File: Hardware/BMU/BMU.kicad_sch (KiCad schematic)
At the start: 5 parts, among them J1 Conn_01x02, J2 Conn_01x04, J3 Conn_01x02, J4 Conn_01x03, J5 Conn_01x03

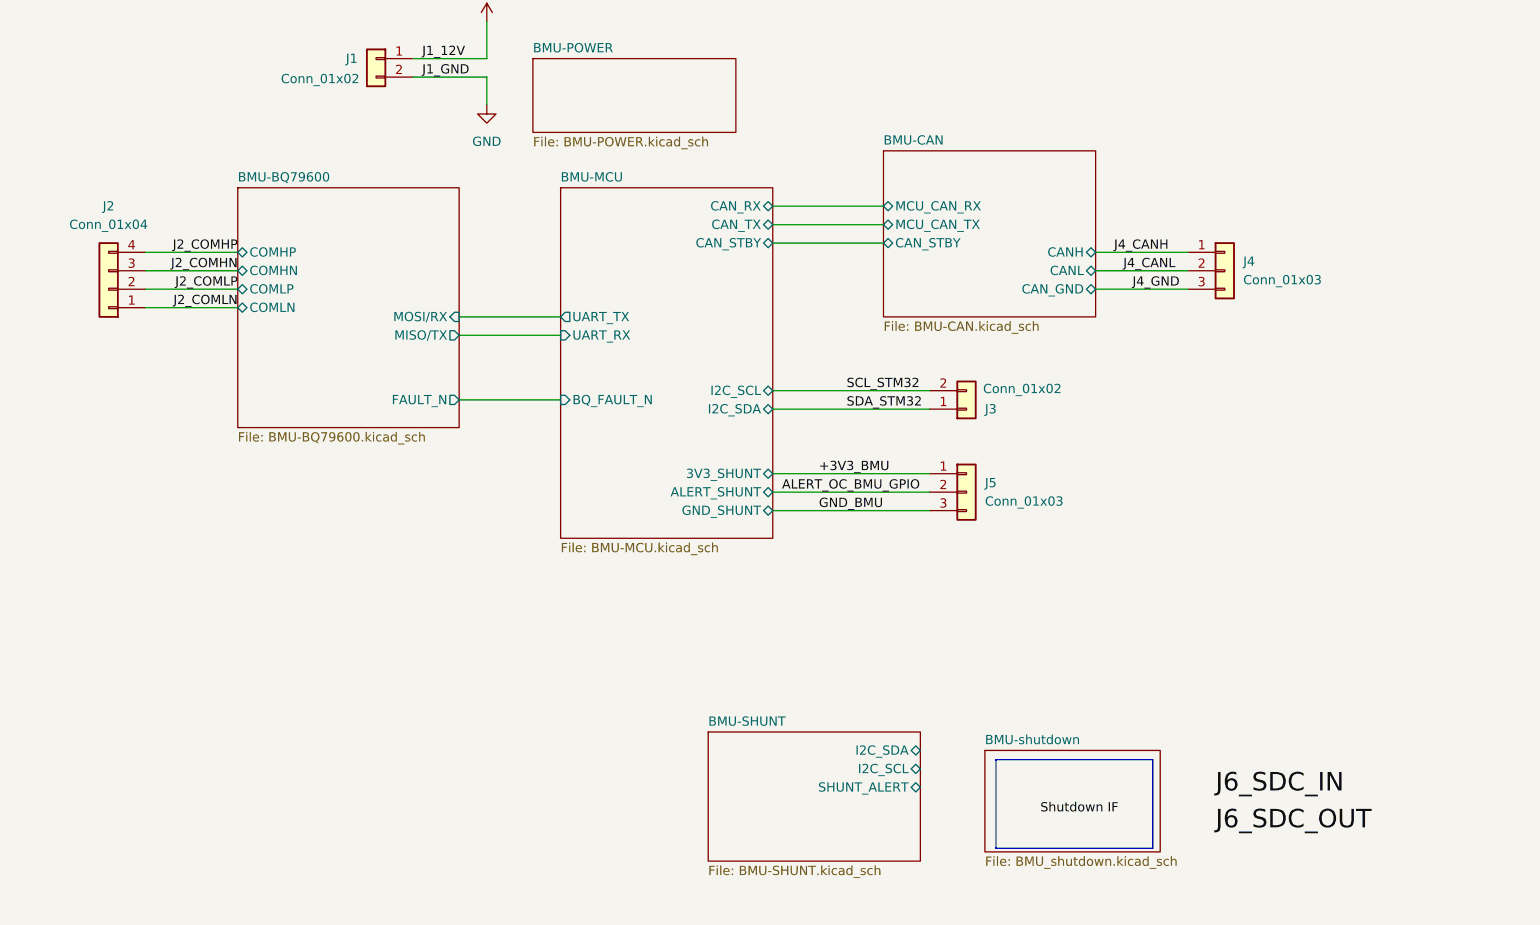
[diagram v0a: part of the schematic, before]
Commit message: change CAN
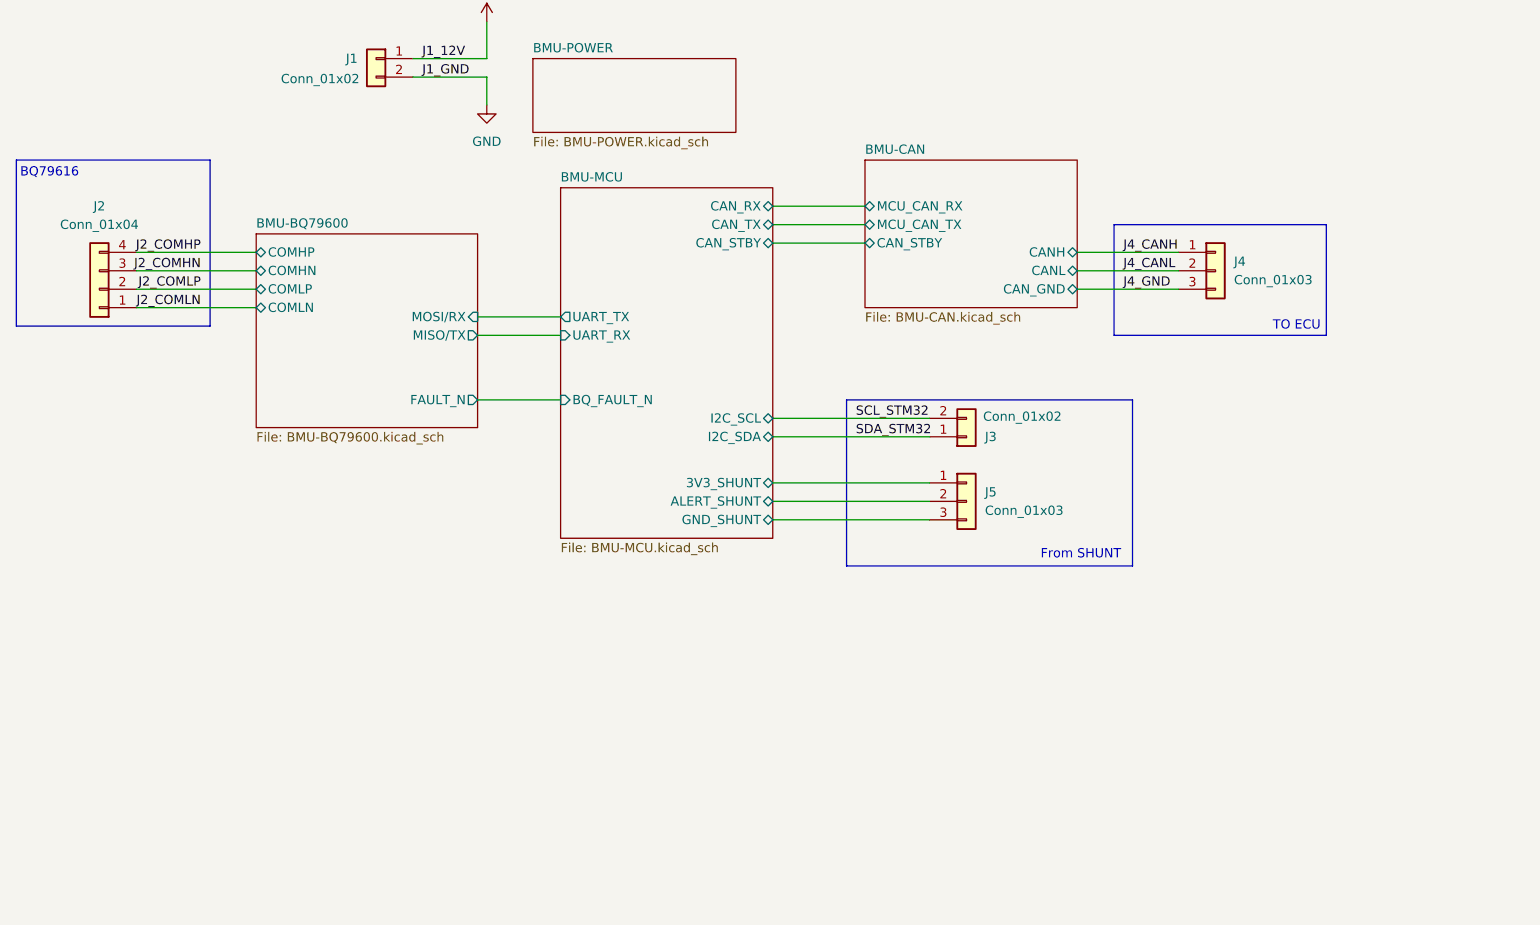
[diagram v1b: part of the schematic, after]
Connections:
- net +3V3_BMU renamed BMU-MCU/3V3_SHUNT
- net ALERT_OC_BMU_GPIO renamed BMU-MCU/ALERT_SHUNT
- net GND_BMU renamed BMU-MCU/GND_SHUNT
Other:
- removed sheet BMU-SHUNT
- removed sheet BMU-shutdown
- note added: "BQ79616"
- note added: "From SHUNT"
- note added: "TO ECU"
- moved on the sheet: J2, J3, J4, J5

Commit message: add comment
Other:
- note added: "1. BMU-POWER Core function: Conditions the 12 V input and generates the regulated 5 V and 3.3 V rails. Short version for page 1: 12 V input conditioning and protection Generates 5 V and 3.3 V rails Supplies power to BMU circuits"
- note added: "2. BMU-MCU Core function: Main STM32 controller for BMU logic, diagnostics, and communications. Short version for page 1: Main STM32 control page Executes BMU control and monitoring logic Interfaces with BQ, CAN, and external shunt board"
- note added: "3. BMU-BQ79600 Core function: Interfaces the MCU with the external battery-monitor daisy-chain network. Short version for page 1: BQ79600 host interface Connects STM32 to external battery monitor chain Handles daisy-chain communication"
- note added: "4. BMU-CAN Core function: Provides the physical CAN-FD bus interface between the BMU and vehicle ECU. Short version for page 1: CAN-FD transceiver interface Converts MCU signals to CAN bus levels Connects BMU to ECU / vehicle network"
- note added: "Optional module, if you keep it later 5. BMU-SAFETY Core function: Routes BMU fault and status signals to external shutdown or safety circuits. Short version for page 1: Safety / shutdown interface Routes fault and status signals Optional external safety path"
- note removed: "1. BMU-POWER Core function: Converts vehicle 12V input into regulated onboard supply rails for all BMU circuits. Short version for page 1: 12V input conditioning and protection Generates regulated 5V and 3.3V rails Distributes power to MCU, CAN, BQ interface, and sensing circuits"
- note removed: "2. BMU-MCU Core function: Acts as the central controller for data processing, diagnostics, and system communication. Short version for page 1: Main STM32 controller Executes BMU control and monitoring logic Communicates with BQ interface, CAN, and current sensing circuits Provides debug and programming access"
- note removed: "3. BMU-BQ79600 Core function: Bridges the MCU host interface to the external battery-monitor daisy-chain communication link. Short version for page 1: BQ79600 host-to-daisy-chain bridge Interfaces STM32 to external BQ79616 module chain Handles battery monitor communication link You can also use this slightly clearer wording: Interfaces the MCU with the external battery monitoring daisy-chain netw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"
- note removed: "4. BMU-CAN Core function: Provides physical CAN-FD bus interface between the BMU and vehicle ECU. Short version for page 1: CAN-FD transceiver interface Converts MCU CAN signals to vehicle bus levels Connects BMU to ECU / vehicle network"
- note removed: "5. BMU-SHUNT Core function: Measures pack current from the external shunt and reports it to the MCU. Short version for page 1: Shunt-based current sensing interface Acquires pack current information Sends current measurement data to MCU"
- note removed: "Optional module, if you keep it later 6. BMU-SAFETY Core function: Interfaces BMU fault/status signals with external shutdown or safety-related control paths. Short version for page 1: Safety and shutdown interface Fault/status signal routing Optional interface to shutdown and indicator circuits"
- moved on the sheet: J1, J2, J3, J4, J5

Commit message: add footprint
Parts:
- J1: value Conn_01x02 -> IN/GND; footprint (none) -> Connector_PinHeader_2.54mm:PinHeader_1x02_P2.54mm_Vertical
- J2: value Conn_01x04 -> COM; footprint (none) -> Connector_PinHeader_2.54mm:PinHeader_1x04_P2.54mm_Vertical
- J3: value Conn_01x02 -> I2C; footprint (none) -> Connector_PinHeader_2.54mm:PinHeader_1x02_P2.54mm_Vertical
- J4: value Conn_01x03 -> CAN; footprint (none) -> Connector_PinHeader_2.54mm:PinHeader_1x03_P2.54mm_Vertical
- J5: value Conn_01x03 -> SHUNT; footprint (none) -> Connector_PinHeader_2.54mm:PinHeader_1x03_P2.54mm_Vertical
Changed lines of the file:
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@@
 			)
 		)
-		(property "Value" "Conn_01x03"
+		(property "Value" "SHUNT"
 			(at 228.6 168.9099 0)
 			(show_name no)
@@
 			)
 		)
-		(property "Footprint" ""
+		(property "Footprint" "Connector_PinHeader_2.54mm:PinHeader_1x03_P2.54mm_Vertical"
 			(at 226.06 167.64 0)
 			(hide yes)
@@
 			)
 		)
-		(property "Value" "Conn_01x04"
+		(property "Value" "COM"
 			(at 106.68 129.54 0)
 			(show_name no)
@@
 			)
 		)
-		(property "Footprint" ""
+		(property "Footprint" "Connector_PinHeader_2.54mm:PinHeader_1x04_P2.54mm_Vertical"
 			(at 106.68 138.43 0)
 			(hide yes)
@@
 			)
 		)
-		(property "Value" "Conn_01x03"
+		(property "Value" "CAN"
 			(at 262.89 137.1599 0)
 			(show_name no)
@@
 			)
 		)
-		(property "Footprint" ""
+		(property "Footprint" "Connector_PinHeader_2.54mm:PinHeader_1x03_P2.54mm_Vertical"
 			(at 260.35 135.89 0)
 			(hide yes)
@@
 			)
 		)
-		(property "Value" "Conn_01x02"
+		(property "Value" "IN/GND"
 			(at 142.494 109.474 0)
 			(show_name no)
@@
 			)
 		)
-		(property "Footprint" ""
+		(property "Footprint" "Connector_PinHeader_2.54mm:PinHeader_1x02_P2.54mm_Vertical"
 			(at 144.78 106.68 0)
 			(hide yes)
@@
 			)
 		)
-		(property "Value" "Conn_01x02"
+		(property "Value" "I2C"
 			(at 228.346 155.956 0)
 			(show_name no)
@@
 			)
 		)
-		(property "Footprint" ""
+		(property "Footprint" "Connector_PinHeader_2.54mm:PinHeader_1x02_P2.54mm_Vertical"
 			(at 226.06 158.75 0)
 			(hide yes)
@@
 	)
 	(sheet
-		(at 166.37 106.68)
-		(size 27.94 10.16)
+		(at 166.37 105.41)
+		(size 27.94 11.43)
 		(exclude_from_sim no)
 		(in_bom yes)
@@
 		)
 		(property "Sheetname" "BMU-POWER"
-			(at 166.37 105.9684 0)
-			(show_name no)
-			(do_not_autoplace no)
+			(at 166.37 104.6984 0)
+			(show_name no)
+			(do_not_autoplace no)

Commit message: add iso
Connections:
- net J2_COMHN renamed COMHN
- net J2_COMHP renamed COMHP
- net J2_COMLN renamed COMLN
- net J2_COMLP renamed COMLP
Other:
- note added: "2. BMU-BQ79600 Core function: Implements the isolated BQ79600 host bridge between the MCU and the external battery-monitor daisy-chain / ring network. Short version for page 1: Isolated BQ79600 host bridge interface Connects STM32 to external battery monitor chain Handles daisy-chain / ring communication"
- note added: "3. BMU-MCU Core function: Main STM32 controller for BMU logic, diagnostics, and communications. Short version for page 1: Main STM32 control page Executes BMU control and monitoring logic Interfaces with BQ, CAN, and external shunt board"
- note added: "ISO"
- note removed: "2. BMU-MCU Core function: Main STM32 controller for BMU logic, diagnostics, and communications. Short version for page 1: Main STM32 control page Executes BMU control and monitoring logic Interfaces with BQ, CAN, and external shunt board"
- note removed: "3. BMU-BQ79600 Core function: Interfaces the MCU with the external battery-monitor daisy-chain network. Short version for page 1: BQ79600 host interface Connects STM32 to external battery monitor chain Handles daisy-chain communication"

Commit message: update
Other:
- sheet BMU-BQ79600 renamed BMU-COM Bridge
- sheet BMU-COM Bridge: file BMU-BQ79600.kicad_sch -> BMU-COM Bridge.kicad_sch
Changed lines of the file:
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@@
 	(rectangle
 		(start 98.044 142.24)
-		(end 115.57 154.686)
+		(end 107.95 153.67)
 		(stroke
 			(width 0)
@@
 			(color 0 0 0 0)
 		)
-		(property "Sheetname" "BMU-BQ79600"
+		(property "Sheetname" "BMU-COM Bridge"
 			(at 130.81 138.9884 0)
 			(show_name no)
@@
 			)
 		)
-		(property "Sheetfile" "BMU-BQ79600.kicad_sch"
+		(property "Sheetfile" "BMU-COM Bridge.kicad_sch"
 			(at 130.81 166.9546 0)
 			(show_name no)

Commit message: update bmu
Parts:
- added J4: LOW SIDE, Connector_PinHeader_2.54mm:PinHeader_1x04_P2.54mm_Vertical, symbol Connector_Generic:Conn_01x04
- J2: value COM -> HIGH SIDE
- renumbered J4 to J7
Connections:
- net COMHN renamed High COMHN
- net COMHP renamed High COMHP
- net COMLN: no longer names the net of J2.1 (Pin_1)
- net COMLP: no longer names the net of J2.2 (Pin_2)
- new net LOW COMLN: J4.1 (Pin_1)
- new net LOW COMLP: J4.2 (Pin_2)
- no-connect marks 0 -> 4
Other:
- sheet BMU-COM Bridge ports: added COMHN_1, COMHP_1, COMLN_2, COMLP_2; removed COMHN, COMHP, COMLN, COMLP
- sheet BMU-MCU ports: added SHUTDOWN_REQ, STATUS_LED; removed none
- note added: "-COM connectors follow the TI EVM 4-pin format for high-side and low-side daisy-chain interfaces. -Each connector carries one differential COM pair only; unused pins are left NC."
- note added: "4 3 2 1"
- note removed: "ISO"
- moved on the sheet: J2

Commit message: layout
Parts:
- removed J2: HIGH SIDE, Connector_PinHeader_2.54mm:PinHeader_1x04_P2.54mm_Vertical, symbol Connector_Generic:Conn_01x04
- removed J4: LOW SIDE, Connector_PinHeader_2.54mm:PinHeader_1x04_P2.54mm_Vertical, symbol Connector_Generic:Conn_01x04
- added J2: HIGH SIDE, CONN_70551-xxxx_04_MOL, symbol 70551-0038:705510038
- added J4: LOW SIDE, CONN_70551-xxxx_04_MOL, symbol 70551-0038:705510038
- added J8: AUX_IO, Connector_PinHeader_2.54mm:PinHeader_1x02_P2.54mm_Vertical, symbol Connector_Generic:Conn_01x02
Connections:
- net BMU-MCU/SHUTDOWN_REQ: now also J8.1 (Pin_1)
- net BMU-MCU/STATUS_LED: now also J8.2 (Pin_2)
- net High COMHN: now also J2.4
- net High COMHP: now also J2.3
- net LOW COMLN: now also J4.1
- net LOW COMLP: now also J4.2
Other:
- sheet BMU-CAN ports: added CAN_RX, CAN_TX; removed MCU_CAN_RX, MCU_CAN_TX
- moved on the sheet: J3, J5
